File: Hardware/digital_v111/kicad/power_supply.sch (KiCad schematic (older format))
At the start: 36 parts, among them P2 CONN_01X03, Q2 NDT2955, U2 MCP1700, U7 LM2672M-5.0, U8 LM358

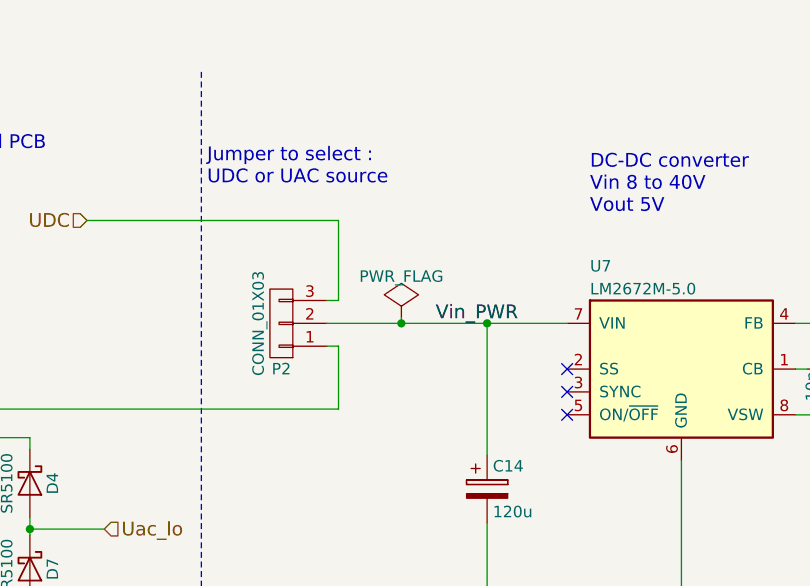
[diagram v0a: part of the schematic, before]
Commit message: move power to powerDC and powerAC
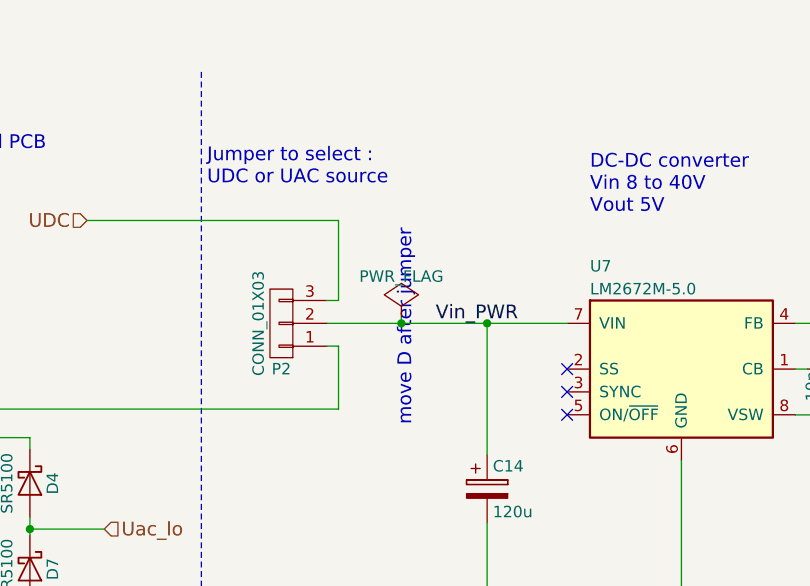
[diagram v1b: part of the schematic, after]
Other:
- note added: "move D after jumper"
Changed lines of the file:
@@
 Text Label 1675 4775 2    60   ~ 0
 Vin_PWR
+Text Notes 3475 2475 1    60   ~ 0
+move D after jumper
 $EndSCHEMATC
